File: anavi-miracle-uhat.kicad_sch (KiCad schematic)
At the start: 20 parts, among them U1 CAT24C32WI-GT3, U2 74LVC1G17W5-7

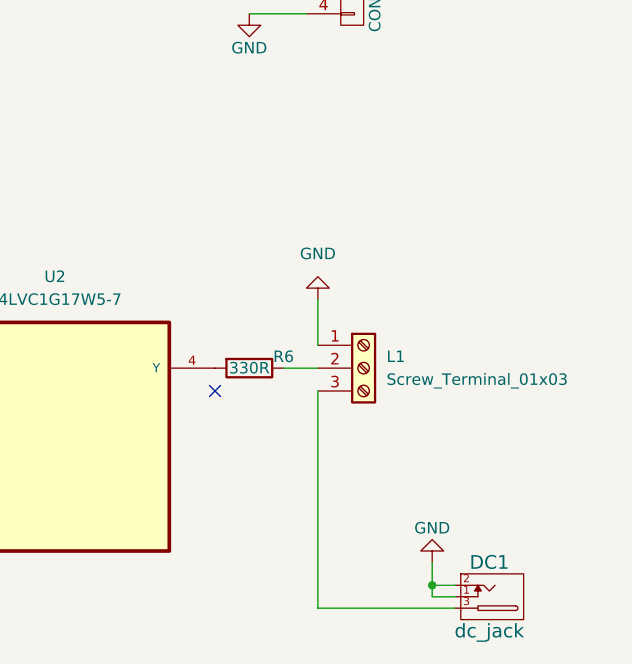
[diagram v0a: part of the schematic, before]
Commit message: anavi-miracle-uhat: Adjust LED strip connector
Adjust the addressable LED strip connector.

Signed-off-by: Leon Anavi <leon@anavi.org>
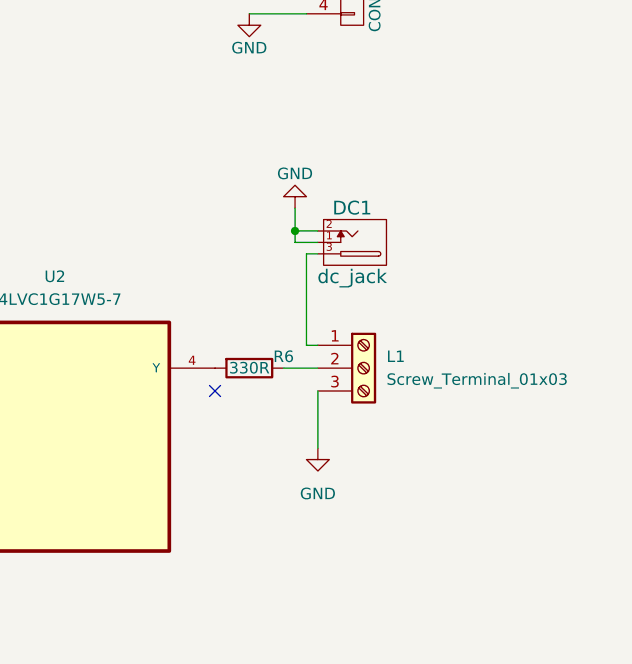
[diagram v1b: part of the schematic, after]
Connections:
- net GND: now also L1.3 (Pin_3); no longer L1.1 (Pin_1)
- net at DC1.3: now also L1.1 (Pin_1); no longer L1.3 (Pin_3)
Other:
- moved on the sheet: DC1
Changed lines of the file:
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@@
   (junction (at 162.56 88.9) (diameter 0) (color 0 0 0 0)
   )
-  (junction (at 237.49 124.46) (diameter 0) (color 0 0 0 0)
+  (junction (at 222.25 85.09) (diameter 0) (color 0 0 0 0)
   )
   (junction (at 85.09 69.85) (diameter 0) (color 0 0 0 0)
@@
     (stroke (width 0) (type default) (color 0 0 0 0))
   )
-  (wire (pts (xy 224.79 127) (xy 240.03 127))
-    (stroke (width 0) (type default) (color 0 0 0 0))
-  )
   (wire (pts (xy 135.89 45.72) (xy 168.91 45.72))
     (stroke (width 0) (type default) (color 0 0 0 0))
@@
     (stroke (width 0) (type default) (color 0 0 0 0))
   )
-  (wire (pts (xy 224.79 102.87) (xy 224.79 127))
-    (stroke (width 0) (type default) (color 0 0 0 0))
-  )
   (wire (pts (xy 162.56 85.09) (xy 162.56 88.9))
     (stroke (width 0) (type default) (color 0 0 0 0))
@@
     (stroke (width 0) (type default) (color 0 0 0 0))
   )
-  (wire (pts (xy 224.79 92.71) (xy 224.79 97.79))
+  (wire (pts (xy 223.52 87.63) (xy 224.79 87.63))
     (stroke (width 0) (type default) (color 0 0 0 0))
   )
@@
     (stroke (width 0) (type default) (color 0 0 0 0))
   )
-  (wire (pts (xy 237.49 124.46) (xy 237.49 121.92))
+  (wire (pts (xy 222.25 85.09) (xy 222.25 82.55))
     (stroke (width 0) (type default) (color 0 0 0 0))
   )
@@
     (stroke (width 0) (type default) (color 0 0 0 0))
   )
-  (wire (pts (xy 237.49 125.73) (xy 237.49 124.46))
+  (wire (pts (xy 222.25 86.36) (xy 222.25 85.09))
     (stroke (width 0) (type default) (color 0 0 0 0))
   )
@@
     (stroke (width 0) (type default) (color 0 0 0 0))
   )
+  (wire (pts (xy 224.79 102.87) (xy 224.79 109.22))
+    (stroke (width 0) (type default) (color 0 0 0 0))
+  )
   (wire (pts (xy 168.91 45.72) (xy 177.8 45.72))
     (stroke (width 0) (type default) (color 0 0 0 0))
@@
     (stroke (width 0) (type default) (color 0 0 0 0))
   )
+  (wire (pts (xy 224.79 97.79) (xy 223.52 97.79))
+    (stroke (width 0) (type default) (color 0 0 0 0))
+  )
   (wire (pts (xy 172.72 33.02) (xy 172.72 48.26))
     (stroke (width 0) (type default) (color 0 0 0 0))
@@
     (stroke (width 0) (type default) (color 0 0 0 0))
   )
-  (wire (pts (xy 240.03 124.46) (xy 237.49 124.46))
+  (wire (pts (xy 224.79 85.09) (xy 222.25 85.09))
     (stroke (width 0) (type default) (color 0 0 0 0))
   )
@@
     (stroke (width 0) (type default) (color 0 0 0 0))
   )
-  (wire (pts (xy 240.03 125.73) (xy 237.49 125.73))
+  (wire (pts (xy 224.79 86.36) (xy 222.25 86.36))
     (stroke (width 0) (type default) (color 0 0 0 0))
   )
@@
   )
   (wire (pts (xy 71.12 93.98) (xy 87.63 93.98))
+    (stroke (width 0) (type default) (color 0 0 0 0))
+  )
+  (wire (pts (xy 223.52 97.79) (xy 223.52 87.63))
     (stroke (width 0) (type default) (color 0 0 0 0))
   )
@@
     (pin "1")
   )
-  (symbol (lib_id "w_connectors:dc_jack") (at 243.84 125.73 0) (unit 1)
-    (in_bom yes) (on_board yes)
-    (property "Reference" "DC1" (id 0) (at 243.84 121.92 0)
-      (effects (font (size 1.524 1.524)))
-    )
-    (property "Value" "dc_jack" (id 1) (at 243.84 129.54 0)
-      (effects (font (size 1.524 1.524)))
-    )
-    (property "Footprint" "w_conn_misc:dc_socket" (id 2) (at 243.84 125.73 0)
+  (symbol (lib_id "w_connectors:dc_jack") (at 228.6 86.36 0) (unit 1)
+    (in_bom yes) (on_board yes)
+    (property "Reference" "DC1" (id 0) (at 228.6 82.55 0)
+      (effects (font (size 1.524 1.524)))
+    )
+    (property "Value" "dc_jack" (id 1) (at 228.6 90.17 0)
+      (effects (font (size 1.524 1.524)))
+    )
+    (property "Footprint" "w_conn_misc:dc_socket" (id 2) (at 228.6 86.36 0)
       (effects (font (size 1.524 1.524)) hide)
     )
-    (property "Datasheet" "" (id 3) (at 243.84 125.73 0)
+    (property "Datasheet" "" (id 3) (at 228.6 86.36 0)
       (effects (font (size 1.524 1.524)))
     )
@@
     (pin "3")
   )
-  (symbol (lib_id "anavi-light-rescue:GND") (at 237.49 121.92 180) (unit 1)
-    (in_bom yes) (on_board yes)
-    (property "Reference" "#PWR018" (id 0) (at 237.49 115.57 0)
-      (effects (font (size 1.27 1.27)) hide)
-    )
-    (property "Value" "GND" (id 1) (at 237.49 118.11 0))
-    (property "Footprint" "" (id 2) (at 237.49 121.92 0))
-    (property "Datasheet" "" (id 3) (at 237.49 121.92 0))
+  (symbol (lib_id "anavi-light-rescue:GND") (at 222.25 82.55 180) (unit 1)
+    (in_bom yes) (on_board yes)
+    (property "Reference" "#PWR018" (id 0) (at 222.25 76.2 0)
+      (effects (font (size 1.27 1.27)) hide)
+    )
+    (property "Value" "GND" (id 1) (at 222.25 78.74 0))
+    (property "Footprint" "" (id 2) (at 222.25 82.55 0))
+    (property "Datasheet" "" (id 3) (at 222.25 82.55 0))
     (pin "1")
   )
@@
     (pin "4")
   )
-  (symbol (lib_id "anavi-miracle-rescue:GND") (at 224.79 92.71 180) (unit 1)
+  (symbol (lib_id "anavi-miracle-rescue:GND") (at 224.79 109.22 0) (unit 1)
     (in_bom yes) (on_board yes) (fields_autoplaced)
-    (property "Reference" "#PWR0101" (id 0) (at 224.79 86.36 0)
-      (effects (font (size 1.27 1.27)) hide)
-    )
-    (property "Value" "GND" (id 1) (at 224.79 87.63 0))
-    (property "Footprint" "" (id 2) (at 224.79 92.71 0))
-    (property "Datasheet" "" (id 3) (at 224.79 92.71 0))
-    (pin "1")
-  )
+    (property "Reference" "#PWR0101" (id 0) (at 224.79 115.57 0)
+      (effects (font (size 1.27 1.27)) hide)
+    )
+    (property "Value" "GND" (id 1) (at 224.79 114.3 0))
+    (property "Footprint" "" (id 2) (at 224.79 109.22 0))
+    (property "Datasheet" "" (id 3) (at 224.79 109.22 0))
+    (pin "1")
+  )
